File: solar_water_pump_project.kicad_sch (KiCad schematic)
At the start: 1 part, among them U1 EFM8BB10F4G-A-QFN20

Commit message: Add files via upload
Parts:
- added U2: RP2040, Package_DFN_QFN:QFN-56-1EP_7x7mm_P0.4mm_EP3.2x3.2mm, symbol MCU_RaspberryPi:RP2040
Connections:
- new net: U2.1 (IOVDD), U2.10 (IOVDD), U2.22 (IOVDD), U2.33 (IOVDD), U2.42 (IOVDD), U2.49 (IOVDD)
- new net: U2.23 (DVDD), U2.50 (DVDD)
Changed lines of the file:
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@@
+    )
+  )
+  (symbol (lib_id "MCU_RaspberryPi:RP2040") (at 74.93 91.44 0) (unit 1)
+    (in_bom yes) (on_board yes) (dnp no) (fields_autoplaced)
+    (property "Reference" "U2" (at 77.1241 135.89 0)
+      (effects (font (size 1.27 1.27)) (justify left))
+    )
+    (property "Value" "RP2040" (at 77.1241 138.43 0)
+      (effects (font (size 1.27 1.27)) (justify left))
+    )
+    (property "Footprint" "Package_DFN_QFN:QFN-56-1EP_7x7mm_P0.4mm_EP3.2x3.2mm" (at 74.93 91.44 0)
+      (effects (font (size 1.27 1.27)) hide)
+    )
+    (property "Datasheet" "https://datasheets.raspberrypi.com/rp2040/rp2040-datasheet.pdf" (at 74.93 91.44 0)
+      (effects (font (size 1.27 1.27)) hide)
+    )
+    (pin "31")
+    (pin "51")
+    (pin "10")
+    (pin "49")
+    (pin "50")
+    (pin "5")
+    (pin "55")
+    (pin "12")
+    (pin "38")
+    (pin "43")
+    (pin "17")
+    (pin "3")
+    (pin "54")
+    (pin "23")
+    (pin "44")
+    (pin "41")
+    (pin "42")
+    (pin "11")
+    (pin "39")
+    (pin "4")
+    (pin "45")
+    (pin "33")
+    (pin "48")
+    (pin "26")
+    (pin "52")
+    (pin "34")
+    (pin "30")
+    (pin "36")
+    (pin "8")
+    (pin "37")
+    (pin "32")
+    (pin "29")
+    (pin "9")
+    (pin "19")
+    (pin "57")
+    (pin "22")
+    (pin "47")
+    (pin "27")
+    (pin "24")
+    (pin "25")
+    (pin "35")
+    (pin "28")
+    (pin "56")
+    (pin "40")
+    (pin "46")
+    (pin "20")
+    (pin "18")
+    (pin "16")
+    (pin "53")
+    (pin "1")
+    (pin "21")
+    (pin "2")
+    (pin "14")
+    (pin "6")
+    (pin "15")
+    (pin "7")
+    (pin "13")
+    (instances
+      (project "solar_water_pump_project"
+        (path "/b825e78c-745a-4fc2-8cc9-f01d0802d2de"
+          (reference "U2") (unit 1)
+        )
+      )
     )
   )

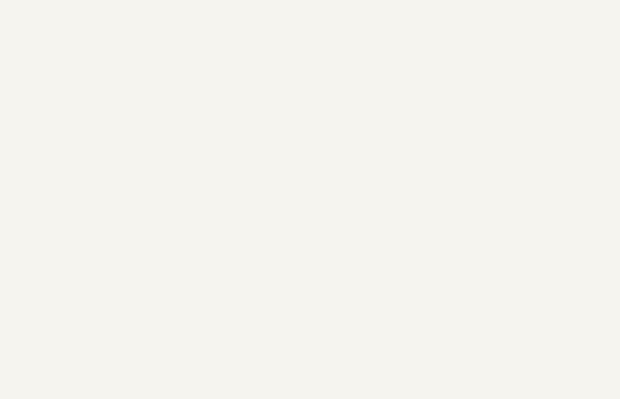
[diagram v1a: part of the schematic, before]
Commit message: added buck converter
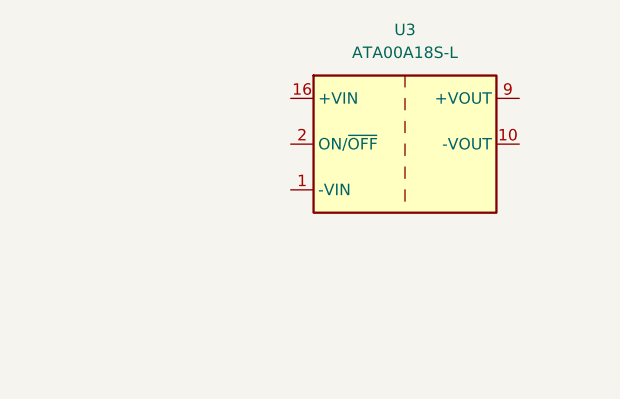
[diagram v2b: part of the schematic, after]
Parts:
- added U3: ATA00A18S-L, Converter_DCDC:Converter_DCDC_Artesyn_ATA_SMD, symbol Converter_DCDC:ATA00A18S-L
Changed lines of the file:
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@@
 (kicad_sch (version 20230121) (generator eeschema)
   (paper "A4")
+  (symbol (lib_id "Converter_DCDC:ATA00A18S-L") (at 147.32 38.1 0) (unit 1)
+    (in_bom yes) (on_board yes) (dnp no) (fields_autoplaced)
+    (property "Reference" "U3" (at 147.32 25.4 0)
+      (effects (font (size 1.27 1.27)))
+    )
+    (property "Value" "ATA00A18S-L" (at 147.32 27.94 0)
+      (effects (font (size 1.27 1.27)))
+    )
+    (property "Footprint" "Converter_DCDC:Converter_DCDC_Artesyn_ATA_SMD" (at 147.32 46.99 0)
+      (effects (font (size 1.27 1.27) italic) hide)
+    )
+    (property "Datasheet" "https://www.artesyn.com/power/assets/ata_series_ds_01apr2015_79c25814fd.pdf" (at 147.32 49.53 0)
+      (effects (font (size 1.27 1.27)) hide)
+    )
+    (pin "9")
+    (pin "10")
+    (pin "16")
+    (pin "2")
+    (pin "1")
+    (pin "8")
+    (pin "7")
+    (instances
+      (project "solar_water_pump_project"
+        (path "/b825e78c-745a-4fc2-8cc9-f01d0802d2de"
+          (reference "U3") (unit 1)
+        )
+      )
+    )
+  )
   (symbol (lib_id "MCU_SiliconLabs:EFM8BB10F4G-A-QFN20") (at 140.97 88.9 0) (unit 1)
     (in_bom yes) (on_board yes) (dnp no) (fields_autoplaced)

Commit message: update
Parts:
- removed U1: EFM8BB10F4G-A-QFN20, Package_DFN_QFN:SiliconLabs_QFN-20-1EP_3x3mm_P0.5mm_EP1.8x1.8mm, symbol MCU_SiliconLabs:EFM8BB10F4G-A-QFN20
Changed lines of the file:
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@@
-    )
-  )
-  (symbol (lib_id "MCU_SiliconLabs:EFM8BB10F4G-A-QFN20") (at 140.97 88.9 0) (unit 1)
-    (in_bom yes) (on_board yes) (dnp no) (fields_autoplaced)
-    (property "Reference" "U1" (at 143.1641 69.85 0)
-      (effects (font (size 1.27 1.27)) (justify left))
-    )
-    (property "Value" "EFM8BB10F4G-A-QFN20" (at 143.1641 72.39 0)
-      (effects (font (size 1.27 1.27)) (justify left))
-    )
-    (property "Footprint" "Package_DFN_QFN:SiliconLabs_QFN-20-1EP_3x3mm_P0.5mm_EP1.8x1.8mm" (at 140.97 68.58 0)
-      (effects (font (size 1.27 1.27)) hide)
-    )
-    (property "Datasheet" "https://www.silabs.com/documents/public/data-sheets/efm8bb1-datasheet.pdf" (at 140.97 88.9 0)
-      (effects (font (size 1.27 1.27)) hide)
-    )
-    (pin "15")
-    (pin "20")
-    (pin "4")
-    (pin "1")
-    (pin "14")
-    (pin "21")
-    (pin "13")
-    (pin "8")
-    (pin "6")
-    (pin "16")
-    (pin "9")
-    (pin "17")
-    (pin "2")
-    (pin "18")
-    (pin "5")
-    (pin "3")
-    (pin "7")
-    (pin "10")
-    (pin "11")
-    (pin "19")
-    (pin "12")
-    (instances
-      (project "solar_water_pump_project"
-        (path "/b825e78c-745a-4fc2-8cc9-f01d0802d2de"
-          (reference "U1") (unit 1)
-        )
-      )
     )
   )

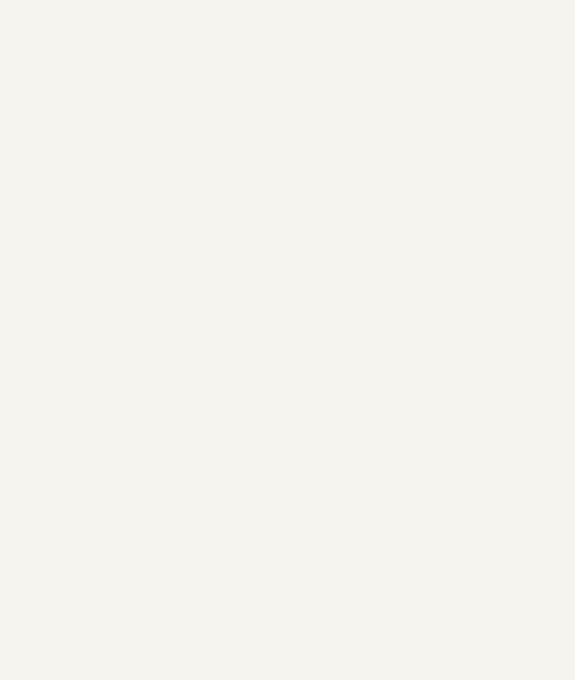
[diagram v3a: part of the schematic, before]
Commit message: Add files via upload
Added power using USB C
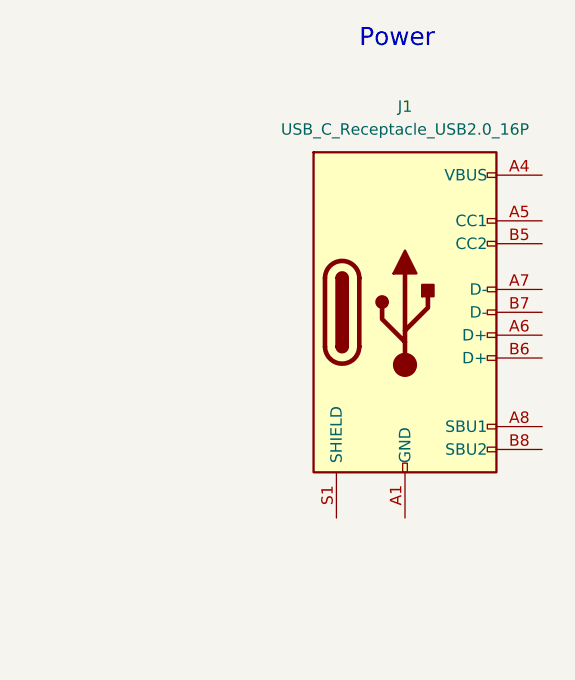
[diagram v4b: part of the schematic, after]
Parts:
- added J1: USB_C_Receptacle_USB2.0_16P, symbol Connector:USB_C_Receptacle_USB2.0_16P
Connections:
- new net: J1.A1 (GND), J1.A12 (GND), J1.B1 (GND), J1.B12 (GND)
- new net: J1.A4 (VBUS), J1.A9 (VBUS), J1.B4 (VBUS), J1.B9 (VBUS)
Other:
- note added: "Power"
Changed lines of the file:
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@@
 (kicad_sch (version 20230121) (generator eeschema)
   (paper "A4")
+  (text "Power" (at 248.92 21.59 0)
+    (effects (font (size 2 2)) (justify left bottom))
+  )
+  (symbol (lib_id "Connector:USB_C_Receptacle_USB2.0_16P") (at 254 50.8 0) (unit 1)
+    (in_bom yes) (on_board yes) (dnp no) (fields_autoplaced)
+    (property "Reference" "J1" (at 254 27.94 0)
+      (effects (font (size 1.27 1.27)))
+    )
+    (property "Value" "USB_C_Receptacle_USB2.0_16P" (at 254 30.48 0)
+      (effects (font (size 1.27 1.27)))
+    )
+    (property "Footprint" "" (at 257.81 50.8 0)
+      (effects (font (size 1.27 1.27)) hide)
+    )
+    (property "Datasheet" "https://www.usb.org/sites/default/files/documents/usb_type-c.zip" (at 257.81 50.8 0)
+      (effects (font (size 1.27 1.27)) hide)
+    )
+    (pin "B6")
+    (pin "B4")
+    (pin "B1")
+    (pin "B12")
+    (pin "A6")
+    (pin "A8")
+    (pin "A5")
+    (pin "A1")
+    (pin "B9")
+    (pin "A7")
+    (pin "A9")
+    (pin "S1")
+    (pin "B5")
+    (pin "B7")
+    (pin "A12")
+    (pin "B8")
+    (pin "A4")
+    (instances
+      (project "solar_water_pump_project"
+        (path "/b825e78c-745a-4fc2-8cc9-f01d0802d2de"
+          (reference "J1") (unit 1)
+        )
+      )
+    )
+  )
   (symbol (lib_id "Converter_DCDC:ATA00A18S-L") (at 147.32 38.1 0) (unit 1)
     (in_bom yes) (on_board yes) (dnp no) (fields_autoplaced)

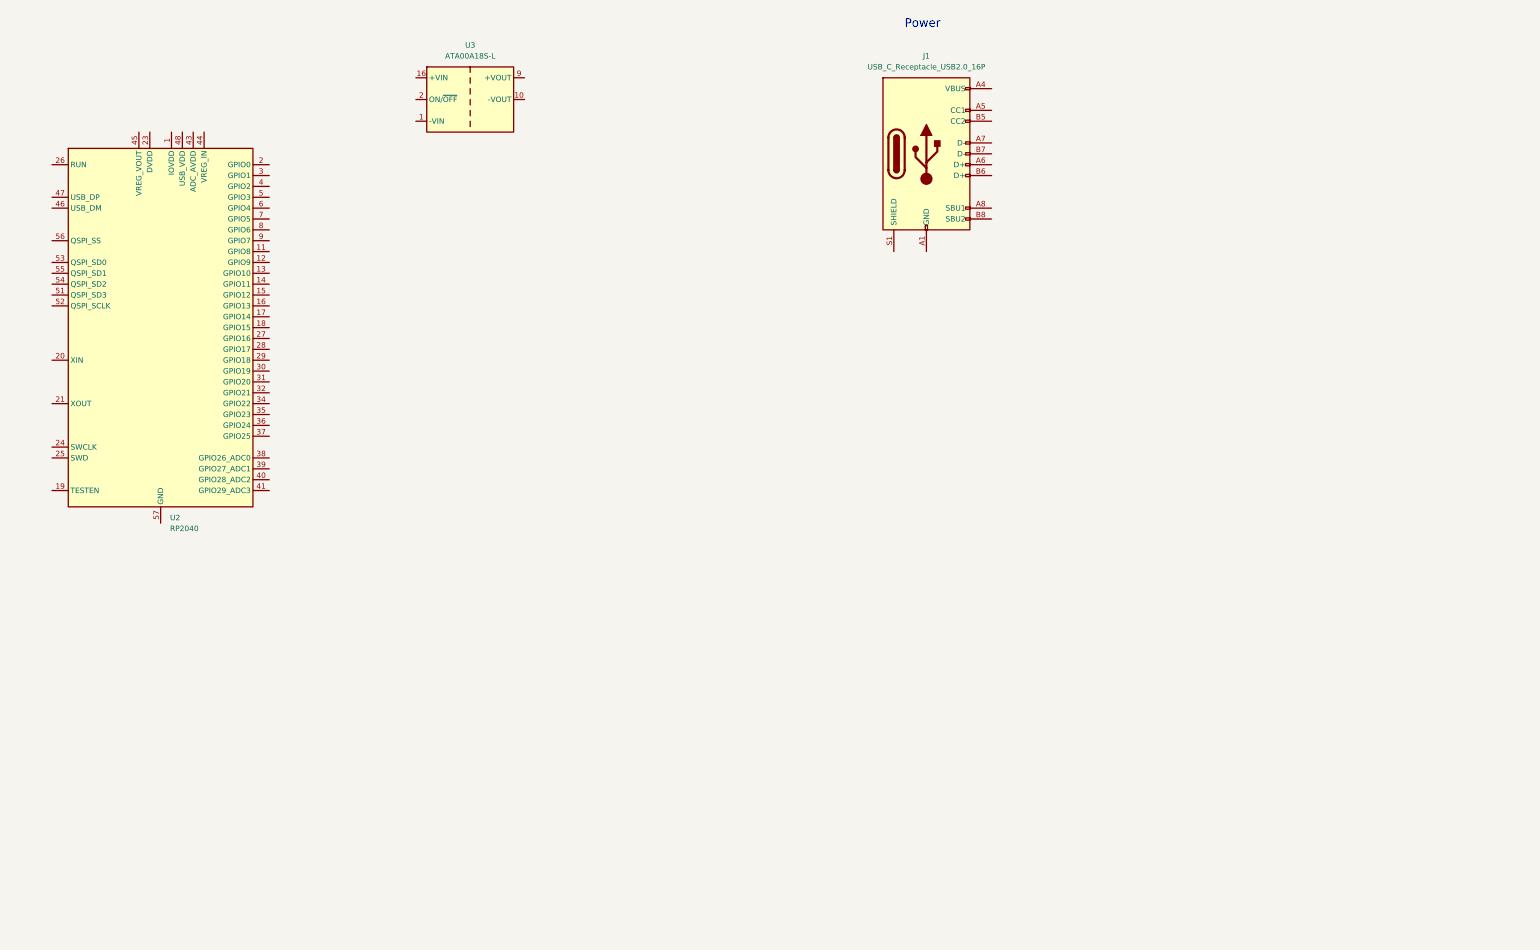
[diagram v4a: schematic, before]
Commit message: updated the power module
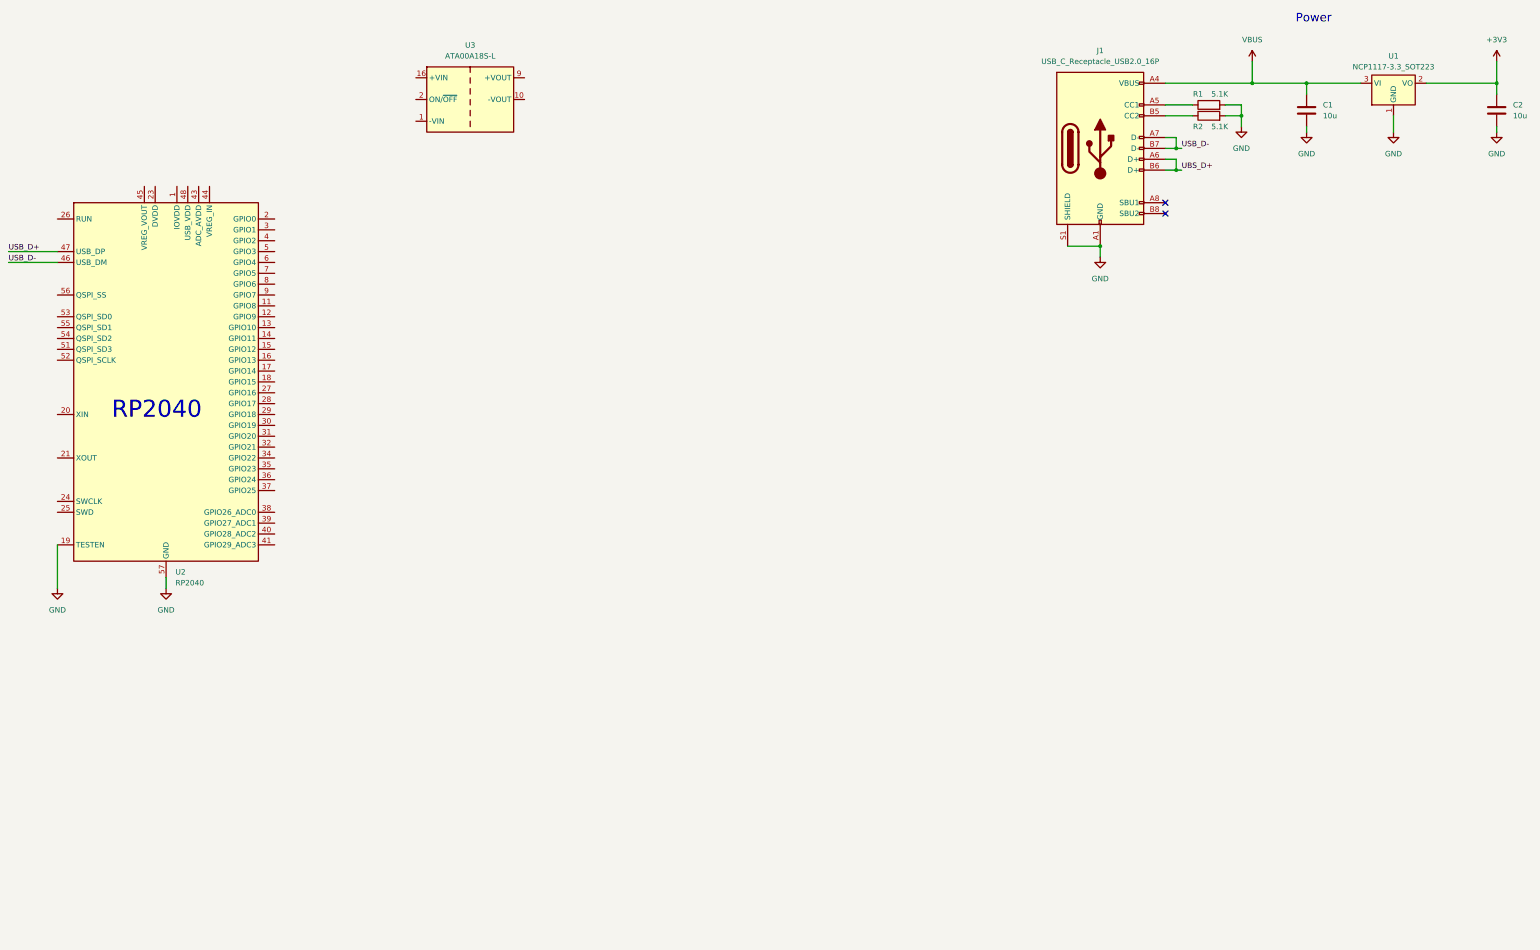
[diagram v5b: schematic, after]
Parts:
- added C1, C2: 10u, symbol Device:C
- added R1, R2: 5.1K, symbol Device:R
- added U1: NCP1117-3.3_SOT223, Package_TO_SOT_SMD:SOT-223-3_TabPin2, symbol Regulator_Linear:NCP1117-3.3_SOT223
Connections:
- net GND: now reaches J1.A1 (GND), J1.A12 (GND), J1.B1 (GND), J1.B12 (GND)
- net GND: now also J1.S1 (SHIELD), U2.19 (TESTEN), U2.57 (GND), C1.2, C2.2, R1.2, R2.2, U1.1 (GND)
- net VBUS: now reaches J1.A4 (VBUS), J1.A9 (VBUS), J1.B4 (VBUS), J1.B9 (VBUS)
- net VBUS: now also C1.1, U1.3 (VI)
- net at J1.A5 (CC1): now also R1.1
- net UBS_D+: now reaches J1.A6 (D+)
- net UBS_D+: now also J1.B6 (D+)
- net USB_D-: now reaches J1.A7 (D-)
- net USB_D-: now also J1.B7 (D-), U2.46 (USB_DM)
- net at J1.B5 (CC2): now also R2.1
- net USB_D+: now reaches U2.47 (USB_DP)
- new net +3V3: C2.1, U1.2 (VO)
- no-connect marks 0 -> 2
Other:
- note added: "RP2040"
- moved on the sheet: J1, U2
